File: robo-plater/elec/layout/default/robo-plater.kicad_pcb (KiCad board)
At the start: 2 copper layers, 12 parts, among them U1 ?, U2 ?, U3 ?

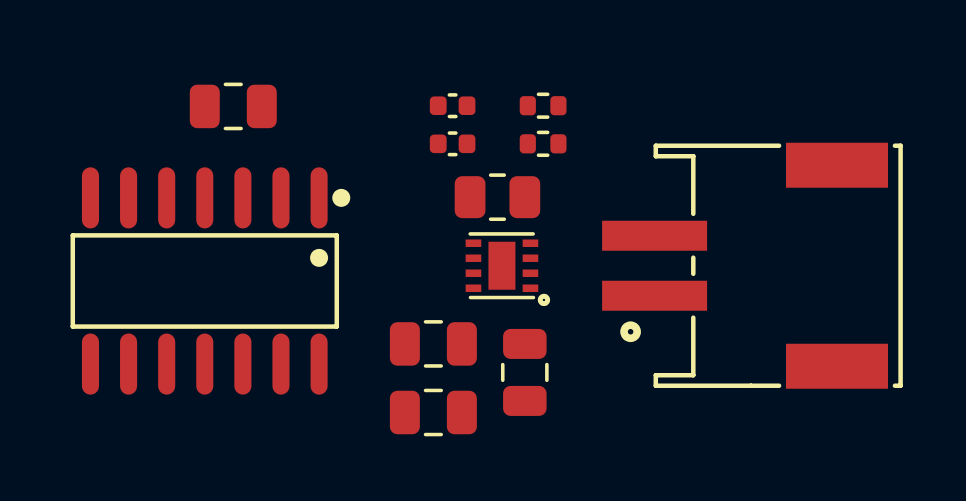
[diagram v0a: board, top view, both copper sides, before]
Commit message: Layout MotorDriver and group layout
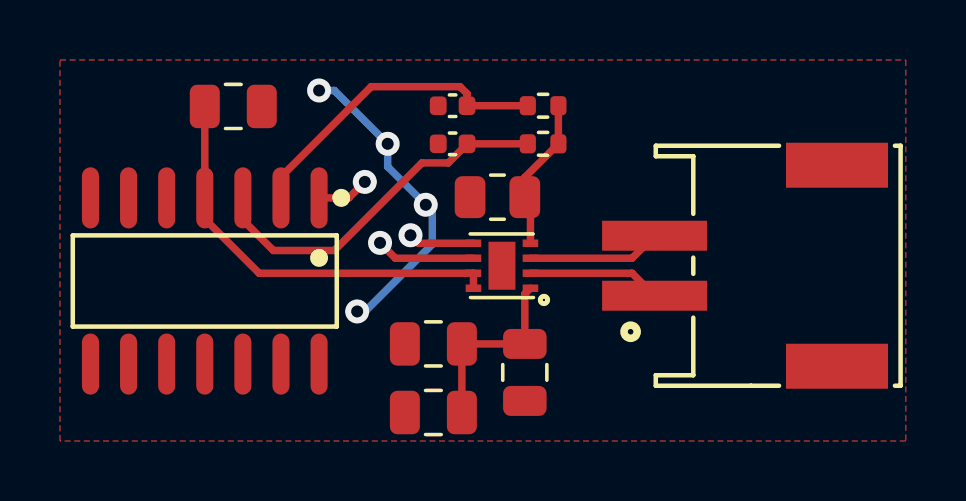
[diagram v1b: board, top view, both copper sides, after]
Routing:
- net ch1-vcc-1: track 0.00 -> 14.0 mm
- net in1_plus: track 0.00 -> 12.1 mm
- net in1_minus: track 0.00 -> 10.7 mm
- net gnd: track 0.00 -> 10.4 mm, vias 0 -> 4
- net ch1-vcc: track 0.00 -> 6.32 mm
- net _shunt_high: track 0.00 -> 5.13 mm
- net out1: track 0.00 -> 4.45 mm
- net ch1.driver-out2: track 0.00 -> 4.45 mm
- net dir: track 0.00 -> 3.33 mm, vias 0 -> 1
- net pwm: track 0.00 -> 2.21 mm, vias 0 -> 1
- net feedback: track 0.00 -> 1.74 mm, vias 0 -> 1
- added copper zone on F.Cu, net gnd

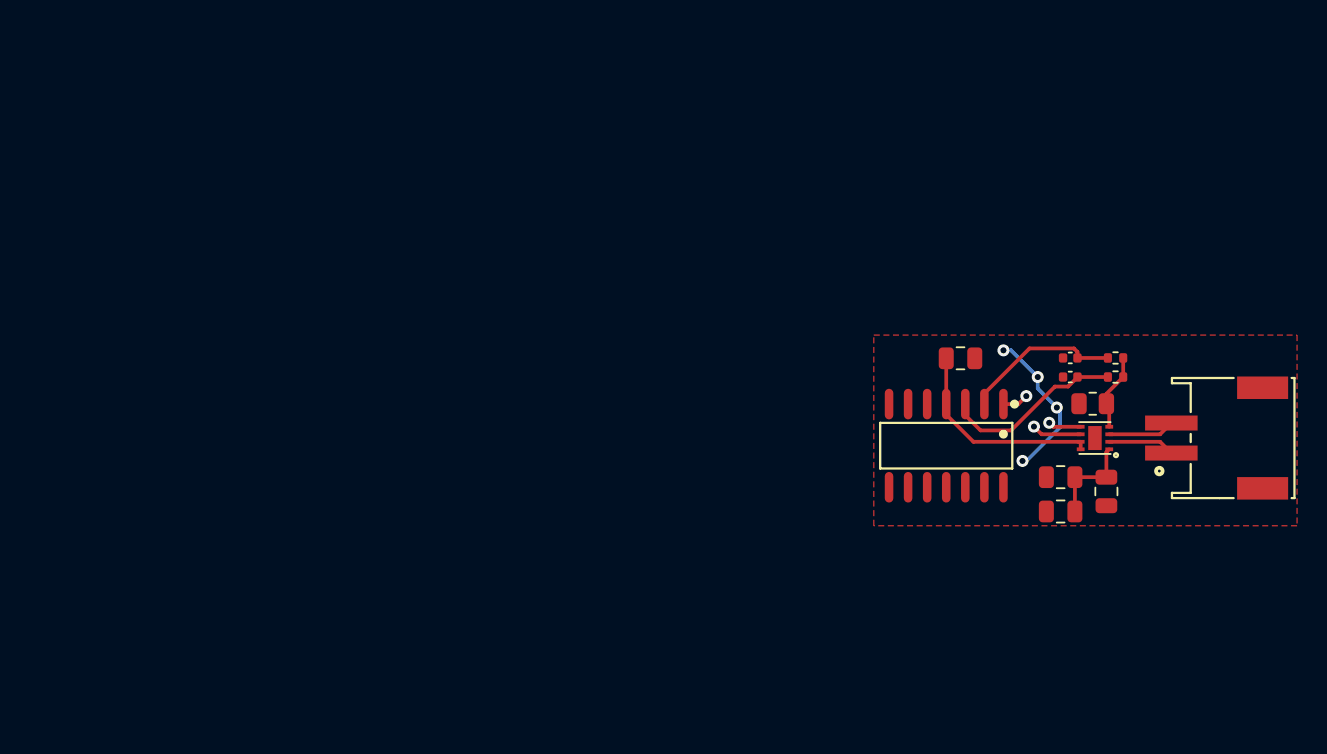
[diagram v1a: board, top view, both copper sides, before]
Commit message: Update feedback circuit
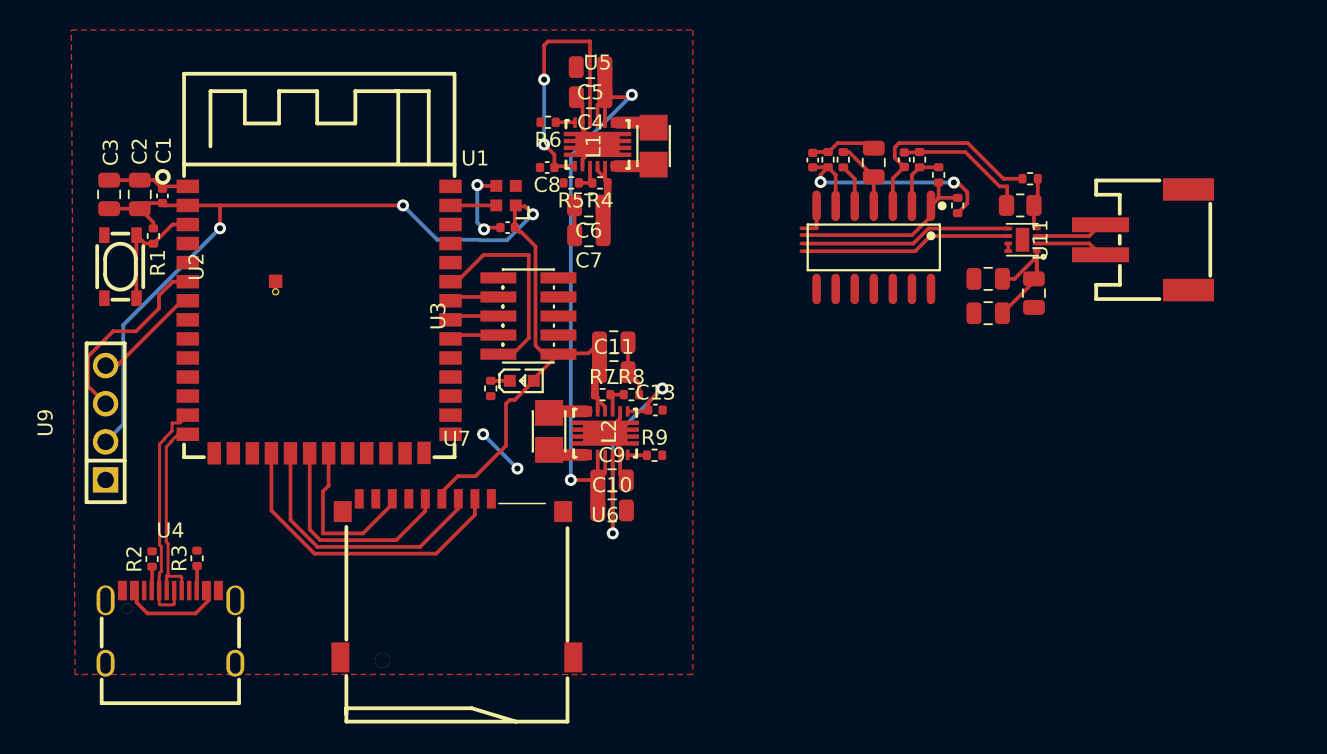
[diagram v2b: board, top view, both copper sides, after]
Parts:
- added C1: 16V 100nF X7R ±10% 0402 Multilayer Ceramic Capacitors MLCC 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, lib:C0402, F.Cu at (109.8, 63.9)
- added C10: 25V 10uF X5R ±10% 0805 Multilayer Ceramic Capacitors MLCC -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, lib:C0805, F.Cu at (139.8, 84.8)
- added C11: 25V 10uF X5R ±10% 0805 Multilayer Ceramic Capacitors MLCC -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, lib:C0805, F.Cu at (139.9, 75.6)
- added C12: 25V 10uF X5R ±10% 0805 Multilayer Ceramic Capacitors MLCC -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, lib:C0805, F.Cu at (139.9, 73.6)
- added C13: 16V 100nF X7R ±10% 0402 Multilayer Ceramic Capacitors MLCC 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, lib:C0402, F.Cu at (142.7, 78.1)
- added C14: 16V 100nF X7R ±10% 0402 Multilayer Ceramic Capacitors MLCC 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, lib:C0402, F.Cu at (132.8, 66.0)
- added C2: 25V 10uF X5R ±10% 0805 Multilayer Ceramic Capacitors MLCC -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, lib:C0805, F.Cu at (108.3, 63.8)
- added C3: 25V 10uF X5R ±10% 0805 Multilayer Ceramic Capacitors MLCC -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, lib:C0805, F.Cu at (106.3, 63.8)
- added C4: 25V 10uF X5R ±10% 0805 Multilayer Ceramic Capacitors MLCC -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, lib:C0805, F.Cu at (138.4, 57.3)
- added C5: 25V 10uF X5R ±10% 0805 Multilayer Ceramic Capacitors MLCC -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, lib:C0805, F.Cu at (138.4, 55.3)
- added C6: 25V 10uF X5R ±10% 0805 Multilayer Ceramic Capacitors MLCC -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, lib:C0805, F.Cu at (138.2, 64.5)
- added C7: 25V 10uF X5R ±10% 0805 Multilayer Ceramic Capacitors MLCC -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, lib:C0805, F.Cu at (138.2, 66.5)
- added C8: 16V 100nF X7R ±10% 0402 Multilayer Ceramic Capacitors MLCC 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, lib:C0402, F.Cu at (135.5, 62.0)
- added C9: 25V 10uF X5R ±10% 0805 Multilayer Ceramic Capacitors MLCC -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, lib:C0805, F.Cu at (139.8, 82.8)
- added L1: ?, lib:IND-SMD_L2.5-W2.0_WPN252012H, F.Cu at (142.6, 60.6)
- added L2: ?, lib:IND-SMD_L2.5-W2.0_WPN252012H, F.Cu at (135.6, 79.6)
- added LED1: ?, lib:LED0603-RD, F.Cu at (133.8, 76.2)
- added R1: 62.5mW Thick Film Resistors 50V ±100ppm/℃ ±1% 10kΩ 0402 Chi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, lib:R0402, F.Cu at (109.2, 66.6)
- added R10: 62.5mW Thick Film Resistors 50V ±100ppm/℃ ±1% 330Ω 0402 Chi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, lib:R0402, F.Cu at (131.7, 76.7)
- added R13: 62.5mW Thick Film Resistors 50V ±100ppm/℃ ±1% 365Ω 0402 Chi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, lib:R0402, F.Cu at (161.5, 62.5)
- added R14: 62.5mW Thick Film Resistors 50V ±100ppm/℃ ±1% 36.5Ω 0402 Ch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, lib:R0402, F.Cu at (160.3, 61.5)
- added R16: 62.5mW Thick Film Resistors 50V ±100ppm/℃ ±1% 1MΩ 0402 Chip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, lib:R0402, F.Cu at (155.2, 61.5)
- added R17: 62.5mW Thick Film Resistors 50V ±100ppm/℃ ±1% 1MΩ 0402 Chip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, lib:R0402, F.Cu at (154.2, 61.5)
- added R2: 62.5mW Thick Film Resistors 50V ±100ppm/℃ ±1% 4.7kΩ 0402 Ch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, lib:R0402, F.Cu at (109.1, 88.1)
- added R3: 62.5mW Thick Film Resistors 50V ±100ppm/℃ ±1% 4.7kΩ 0402 Ch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, lib:R0402, F.Cu at (112.1, 88.0)
- added R4: 62.5mW 50V ±100ppm/℃ ±1% 25.5kΩ 0402 Chip Resistor - Surfac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, lib:R0402, F.Cu at (139.0, 63.0)
- added R5: 62.5mW Thick Film Resistors 50V ±1% ±200ppm/℃ 2.8kΩ 0402 Ch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, lib:R0402, F.Cu at (137.1, 63.0)
- added R6: 62.5mW Thick Film Resistors 50V ±100ppm/℃ ±1% 1MΩ 0402 Chip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, lib:R0402, F.Cu at (135.5, 59.0)
- added R7: 62.5mW Thick Film Resistors 50V ±100ppm/℃ ±1% 23.7kΩ 0402 C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, lib:R0402, F.Cu at (139.2, 77.1)
- added R8: 62.5mW Thick Film Resistors 50V ±100ppm/℃ ±1% 4.3kΩ 0402 Ch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, lib:R0402, F.Cu at (141.1, 77.1)
- added R9: 62.5mW Thick Film Resistors 50V ±100ppm/℃ ±1% 1MΩ 0402 Chip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, lib:R0402, F.Cu at (142.6, 81.2)
- added U1: ?, lib:WIRELM-SMD_ESP32-S3-WROOM-1, F.Cu at (120.3, 72.1)
- added U12: ?, lib:NetTie-2_SMD_Pad0.25mm, F.Cu at (165.6, 63.2)
- added U2: ?, lib:KEY-SMD_4P-L4.2-W3.2-P2.20-LS4.6, F.Cu at (107.0, 68.6)
- added U3: ?, lib:HDR-SMD_10P-P1.27-V-M-R2-C5-LS5.3, F.Cu at (134.2, 71.9)
- added U4: ?, lib:USB-C-SMD_KH-TYPE-C-16P, F.Cu at (110.4, 92.6)
- added U5: ?, lib:VSON-14_L4.0-W3.0-P0.50-BL-EP_TI_DSJ, F.Cu at (138.8, 60.5)
- added U6: ?, lib:VSON-14_L4.0-W3.0-P0.50-BL-EP_TI_DSJ, F.Cu at (139.3, 79.7)
- added U7: ?, lib:TF-SMD_TF-01A, F.Cu at (129.5, 89.3)
- added U8: ?, lib:LED-SMD_4P-L2.0-W2.0-BR, F.Cu at (132.7, 63.9)
- added U9: ?, lib:HDR-TH_4P-P2.54-V-F, F.Cu at (106.1, 79.0)
- U11: renamed from U2; footprint lib:CONN-SMD_PH-2AWB -> lib:CONN-SMD_P2.00_S2B-PH-SM4-TB-LF-SN
- moved C20 21.6 mm to (153.2, 61.5), turned to 90 degrees
- moved C19 18.2 mm to (159.3, 61.5), turned to 90 degrees
- moved R15 14.6 mm to (162.8, 64.5), turned to -90 degrees
- moved R12 14.4 mm to (167.6, 62.7)
- moved C18 14.3 mm to (157.2, 61.7), turned to 90 degrees
- moved U11 14.1 mm to (175.3, 66.8)
- moved C15 14.1 mm to (164.8, 71.7)
- moved C16 14.1 mm to (164.8, 69.4)
- moved C17 14.1 mm to (167.9, 70.4)
- moved R11 14.1 mm to (167.0, 64.5)
- moved U10 14.1 mm to (167.1, 66.8)
- moved U13 14.1 mm to (157.2, 67.3)
- renumbered C1 to C15, C2 to C16, C3 to C17, C4 to C18, C5 to C19, C6 to C20, R1 to R11, R2 to R12, R3 to R15, U1 to U10, U3 to U13
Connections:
- net ch1.driver-out2 renamed out2
- C15 pad 2: gnd -> ch1-gnd
- C16 pad 2: gnd -> ch1-gnd
- C17 pad 2: gnd -> ch1-gnd
- C18 pad 2: gnd -> ch1-gnd
- C19 pad 2: gnd -> _shunt_gnd
- C20 pad 1: in1_minus -> in2_minus
- C20 pad 2: gnd -> ch1-gnd
- R11 pad 2: gnd -> ch1-gnd
- R15 pad 1: _shunt_high -> current
- R15 pad 2: in1_minus -> in2_minus
- U13 pad 1: feedback -> current
- U13 pad 11: gnd -> ch1-gnd
- U13 pad 7: ch1.op_amp-out2 -> pulses
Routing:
- net uc.uc.ic-vcc: track 0.00 -> 86.9 mm, vias 0 -> 3
- net uc-vcc: track 0.00 -> 42.3 mm, vias 0 -> 2
- net uc.uc.ic-gnd: track 0.00 -> 28.1 mm, vias 0 -> 2
- net cs: track 0.00 -> 20.7 mm
- net uc._3v3_reg.ic-vina: track 0.00 -> 19.5 mm, vias 0 -> 2
- net uc._5v_reg.ic-vina: track 0.00 -> 18.4 mm, vias 0 -> 2
- net mosi: track 0.00 -> 18.1 mm
- net in2_minus: track 0.00 -> 16.7 mm, vias 0 -> 2
- net usb-: track 0.00 -> 15.7 mm
- net sck: track 0.00 -> 14.7 mm
- net usb+: track 0.00 -> 14.3 mm
- net tms: track 0.00 -> 14.0 mm
- net current: track 0.00 -> 13.6 mm
- net scl: track 0.00 -> 12.8 mm
- net pwm: track 2.21 -> 14.2 mm, vias 1 -> 0
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- added copper zone on F.Cu, net uc.uc.ic-gnd
- removed copper zone on F.Cu, net gnd

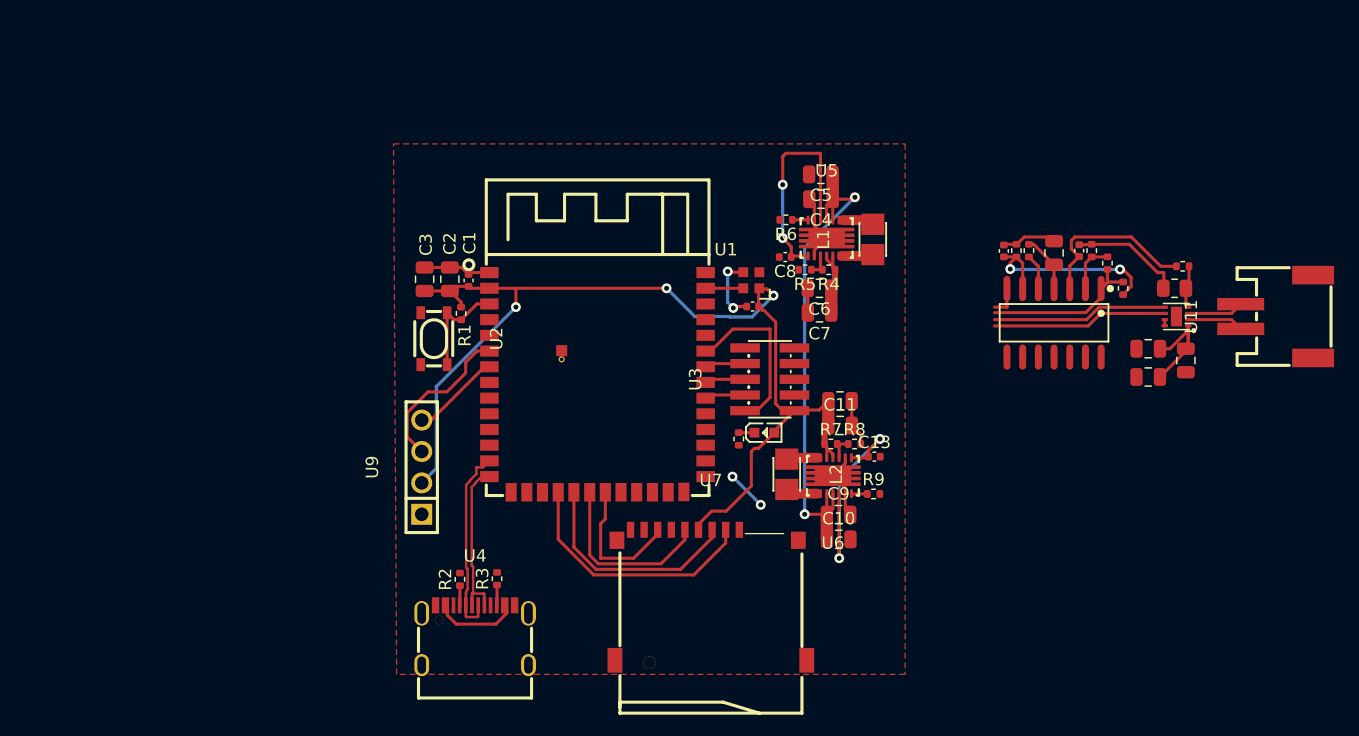
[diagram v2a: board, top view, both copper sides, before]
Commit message: Two motor driver channels with debug headers
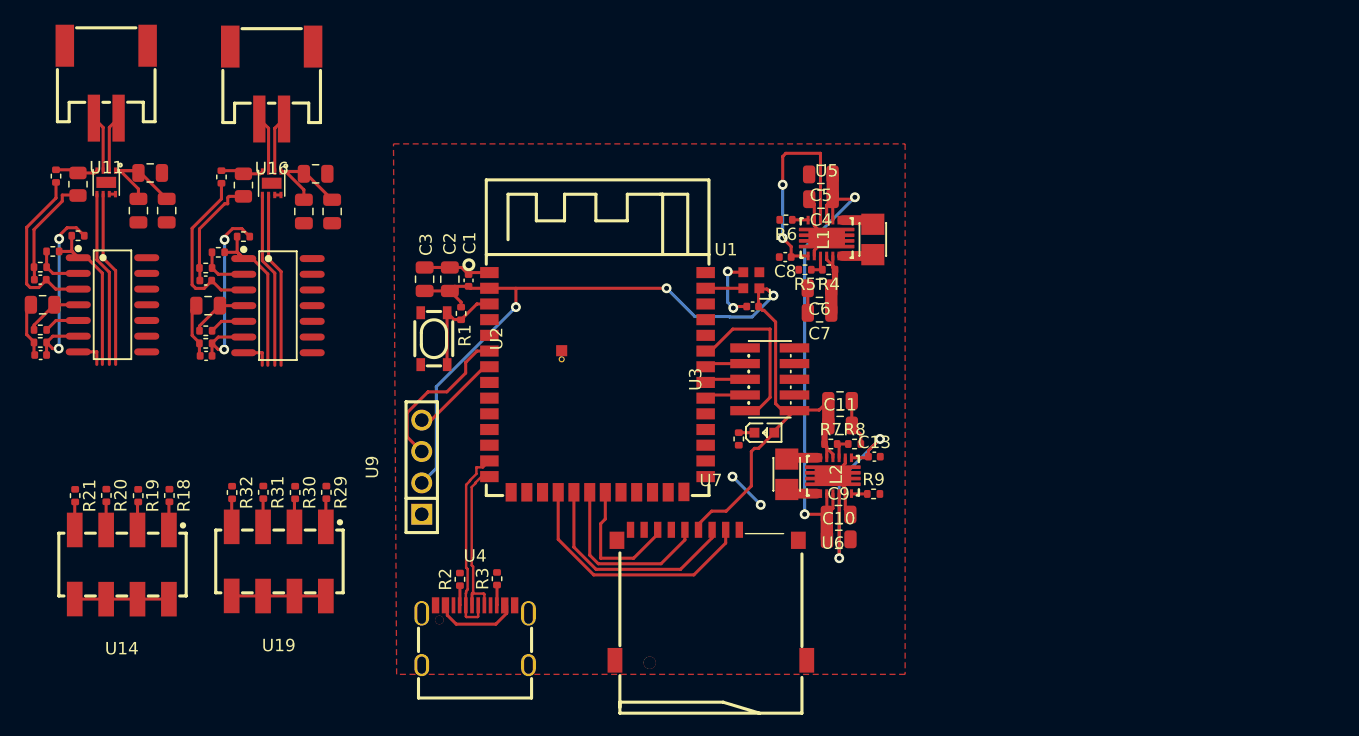
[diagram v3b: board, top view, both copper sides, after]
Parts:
- added C21: 25V 10uF X5R ±10% 0805 Multilayer Ceramic Capacitors MLCC -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, lib:C0805, F.Cu at (98.8, 58.3)
- added C22: 25V 10uF X5R ±10% 0805 Multilayer Ceramic Capacitors MLCC -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, lib:C0805, F.Cu at (96.5, 58.3)
- added C23: 25V 10uF X5R ±10% 0805 Multilayer Ceramic Capacitors MLCC -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, lib:C0805, F.Cu at (97.5, 55.3)
- added C24: 25V 10uF X5R ±10% 0805 Multilayer Ceramic Capacitors MLCC -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, lib:C0805, F.Cu at (88.8, 65.9)
- added C25: 16V 100nF X7R ±10% 0402 Multilayer Ceramic Capacitors MLCC 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, lib:C0402, F.Cu at (88.6, 63.9)
- added C26: 25V 1uF X5R ±10% 0402 Multilayer Ceramic Capacitors MLCC - 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, lib:C0402, F.Cu at (88.6, 70.0)
- added R18: 62.5mW Thick Film Resistors 50V ±100ppm/℃ ±1% 1kΩ 0402 Chip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, lib:R0402, F.Cu at (85.6, 81.3)
- added R19: 62.5mW Thick Film Resistors 50V ±100ppm/℃ ±1% 1kΩ 0402 Chip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, lib:R0402, F.Cu at (83.1, 81.3)
- added R20: 62.5mW Thick Film Resistors 50V ±100ppm/℃ ±1% 1kΩ 0402 Chip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, lib:R0402, F.Cu at (80.5, 81.3)
- added R21: 62.5mW Thick Film Resistors 50V ±100ppm/℃ ±1% 1kΩ 0402 Chip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, lib:R0402, F.Cu at (78.0, 81.3)
- added R22: 125mW Thick Film Resistors 150V ±1% ±400ppm/℃ 1Ω 0805 Chip 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, lib:R0805, F.Cu at (91.6, 56.2)
- added R23: 62.5mW Thick Film Resistors 50V ±100ppm/℃ ±1% 1.33kΩ 0402 C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, lib:R0402, F.Cu at (89.8, 55.5)
- added R24: 62.5mW Thick Film Resistors 50V ±100ppm/℃ ±1% 365Ω 0402 Chi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, lib:R0402, F.Cu at (89.6, 61.6)
- added R25: 62.5mW Thick Film Resistors 50V ±100ppm/℃ ±1% 36.5Ω 0402 Ch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, lib:R0402, F.Cu at (88.6, 62.9)
- added R26: 62.5mW Thick Film Resistors 50V ±100ppm/℃ ±1% 1.05kΩ 0402 C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, lib:R0402, F.Cu at (91.6, 60.3)
- added R27: 62.5mW Thick Film Resistors 50V ±100ppm/℃ ±1% 1MΩ 0402 Chip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, lib:R0402, F.Cu at (88.6, 68.0)
- added R28: 62.5mW Thick Film Resistors 50V ±100ppm/℃ ±1% 1MΩ 0402 Chip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, lib:R0402, F.Cu at (88.6, 69.0)
- added R29: 62.5mW Thick Film Resistors 50V ±100ppm/℃ ±1% 1kΩ 0402 Chip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, lib:R0402, F.Cu at (98.3, 81.0)
- added R30: 62.5mW Thick Film Resistors 50V ±100ppm/℃ ±1% 1kΩ 0402 Chip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, lib:R0402, F.Cu at (95.8, 81.0)
- added R31: 62.5mW Thick Film Resistors 50V ±100ppm/℃ ±1% 1kΩ 0402 Chip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, lib:R0402, F.Cu at (93.2, 81.0)
- added R32: 62.5mW Thick Film Resistors 50V ±100ppm/℃ ±1% 1kΩ 0402 Chip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, lib:R0402, F.Cu at (90.7, 81.0)
- added U14: ?, lib:HDR-SMD_8P-P2.54-V-M-R2-C4-LS7.4, F.Cu at (81.8, 86.9)
- added U15: ?, lib:WSON-8_L2.0-W2.0-P0.50-TL-EP, F.Cu at (93.9, 56.0)
- added U16: ?, lib:CONN-SMD_P2.00_S2B-PH-SM4-TB-LF-SN, F.Cu at (93.9, 47.9)
- added U17: ?, lib:NetTie-2_SMD_Pad0.25mm, F.Cu at (90.4, 57.7)
- added U18: ?, lib:SOIC-14_L8.7-W3.9-P1.27-LS6.0-BL, F.Cu at (94.4, 65.9)
- added U19: ?, lib:HDR-SMD_8P-P2.54-V-M-R2-C4-LS7.4, F.Cu at (94.5, 86.6)
- moved U11 96.6 mm to (80.5, 47.8), turned to 180 degrees
- moved R12 91.5 mm to (76.5, 55.4), turned to -90 degrees
- moved R11 89.1 mm to (78.2, 56.1), turned to -90 degrees
- moved U12 88.8 mm to (77.0, 57.5), turned to 90 degrees
- moved U10 87.3 mm to (80.5, 55.9), turned to -90 degrees
- moved R13 85.3 mm to (76.2, 61.5), turned to 180 degrees
- moved C17 85.2 mm to (84.1, 55.2), turned to 0 degrees
- moved R14 85.1 mm to (75.2, 62.8), turned to 180 degrees
- moved R15 84.7 mm to (78.2, 60.3), turned to 0 degrees
- moved C19 84.1 mm to (75.2, 63.8), turned to 180 degrees
- moved C16 82.5 mm to (83.1, 58.2), turned to -90 degrees
- moved C18 82.0 mm to (75.4, 65.9), turned to 180 degrees
- moved C15 80.6 mm to (85.4, 58.2), turned to -90 degrees
- moved R16 80.3 mm to (75.2, 67.9), turned to 180 degrees
- moved R17 79.3 mm to (75.2, 68.9), turned to 180 degrees
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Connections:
- net _7 renamed uc.jtag.connector-_7
- net _shunt_gnd renamed ch1._shunt_nettie-_shunt_gnd
- net _shunt_high renamed ch1.driver-_shunt_high
- net ch1-gnd renamed gnd
- net ch1-vcc renamed vcc
- net ch1-vcc-1 renamed vcc-1
- net current renamed uc.uc.ic-dp-1
- net dir renamed uc.uc.ic-sda-1
- net ep renamed ch1.driver-ep
- net in1_minus renamed ch1.op_amp-in1_minus
- net in1_plus renamed ch1.op_amp-in1_plus
- net in2_minus renamed ch1.op_amp-in2_minus
- net in2_plus renamed ch1.op_amp-in2_plus
- net in3_minus renamed ch1.op_amp-in3_minus
- net in3_plus renamed ch1.op_amp-in3_plus
- net in4_minus renamed ch1.op_amp-in4_minus
- net in4_plus renamed ch1.op_amp-in4_plus
- net out1 renamed ch1.driver-out1
- net out2 renamed ch1.driver-out2
- net out3 renamed ch1.op_amp-out3
- net out4 renamed ch1.op_amp-out4
- net pulses renamed uc.uc.ic-dm-1
- net pwm renamed uc.uc.ic-scl-1
- net scl renamed uc.uc.ic-scl-2
- net sda renamed uc.uc.ic-sda-2
- U1 pad 10: io17 -> uc.uc.ic-dm
- U1 pad 11: io18 -> uc.uc.ic-dp
- U1 pad 12: io8 -> uc.uc.ic-sda
- U1 pad 15: io3 -> uc.uc.ic-scl
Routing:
- net gnd: track 5.76 -> 26.9 mm
- net ch2.op_amp-in2_minus: track 0.00 -> 16.7 mm, vias 0 -> 2
- net uc.uc.ic-sda: track 0.00 -> 14.2 mm
- net uc.uc.ic-scl: track 0.00 -> 14.2 mm
- net ch2.op_amp-in1_plus: track 0.00 -> 14.1 mm
- net uc.uc.ic-dp: track 0.00 -> 13.6 mm
- net vcc: track 10.0 -> 20.1 mm
- net ch2._shunt_nettie-_shunt_gnd: track 0.00 -> 7.32 mm
- net vcc-1: track 5.15 -> 10.3 mm
- net ch2.driver-out2: track 0.00 -> 4.56 mm
- net ch2.driver-out1: track 0.00 -> 4.56 mm
- net ch2.op_amp-in1_minus: track 0.00 -> 4.04 mm
- net ch2.driver-_shunt_high: track 0.00 -> 3.50 mm
- net ch2.op_amp-in2_plus: track 0.00 -> 2.88 mm
- net uc.uc.ic-dm: track 0.00 -> 2.52 mm
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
